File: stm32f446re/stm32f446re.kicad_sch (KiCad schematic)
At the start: 15 parts, among them SW1 SW_Push, SW2 SW_SPDT, U1 STM32F446RETx

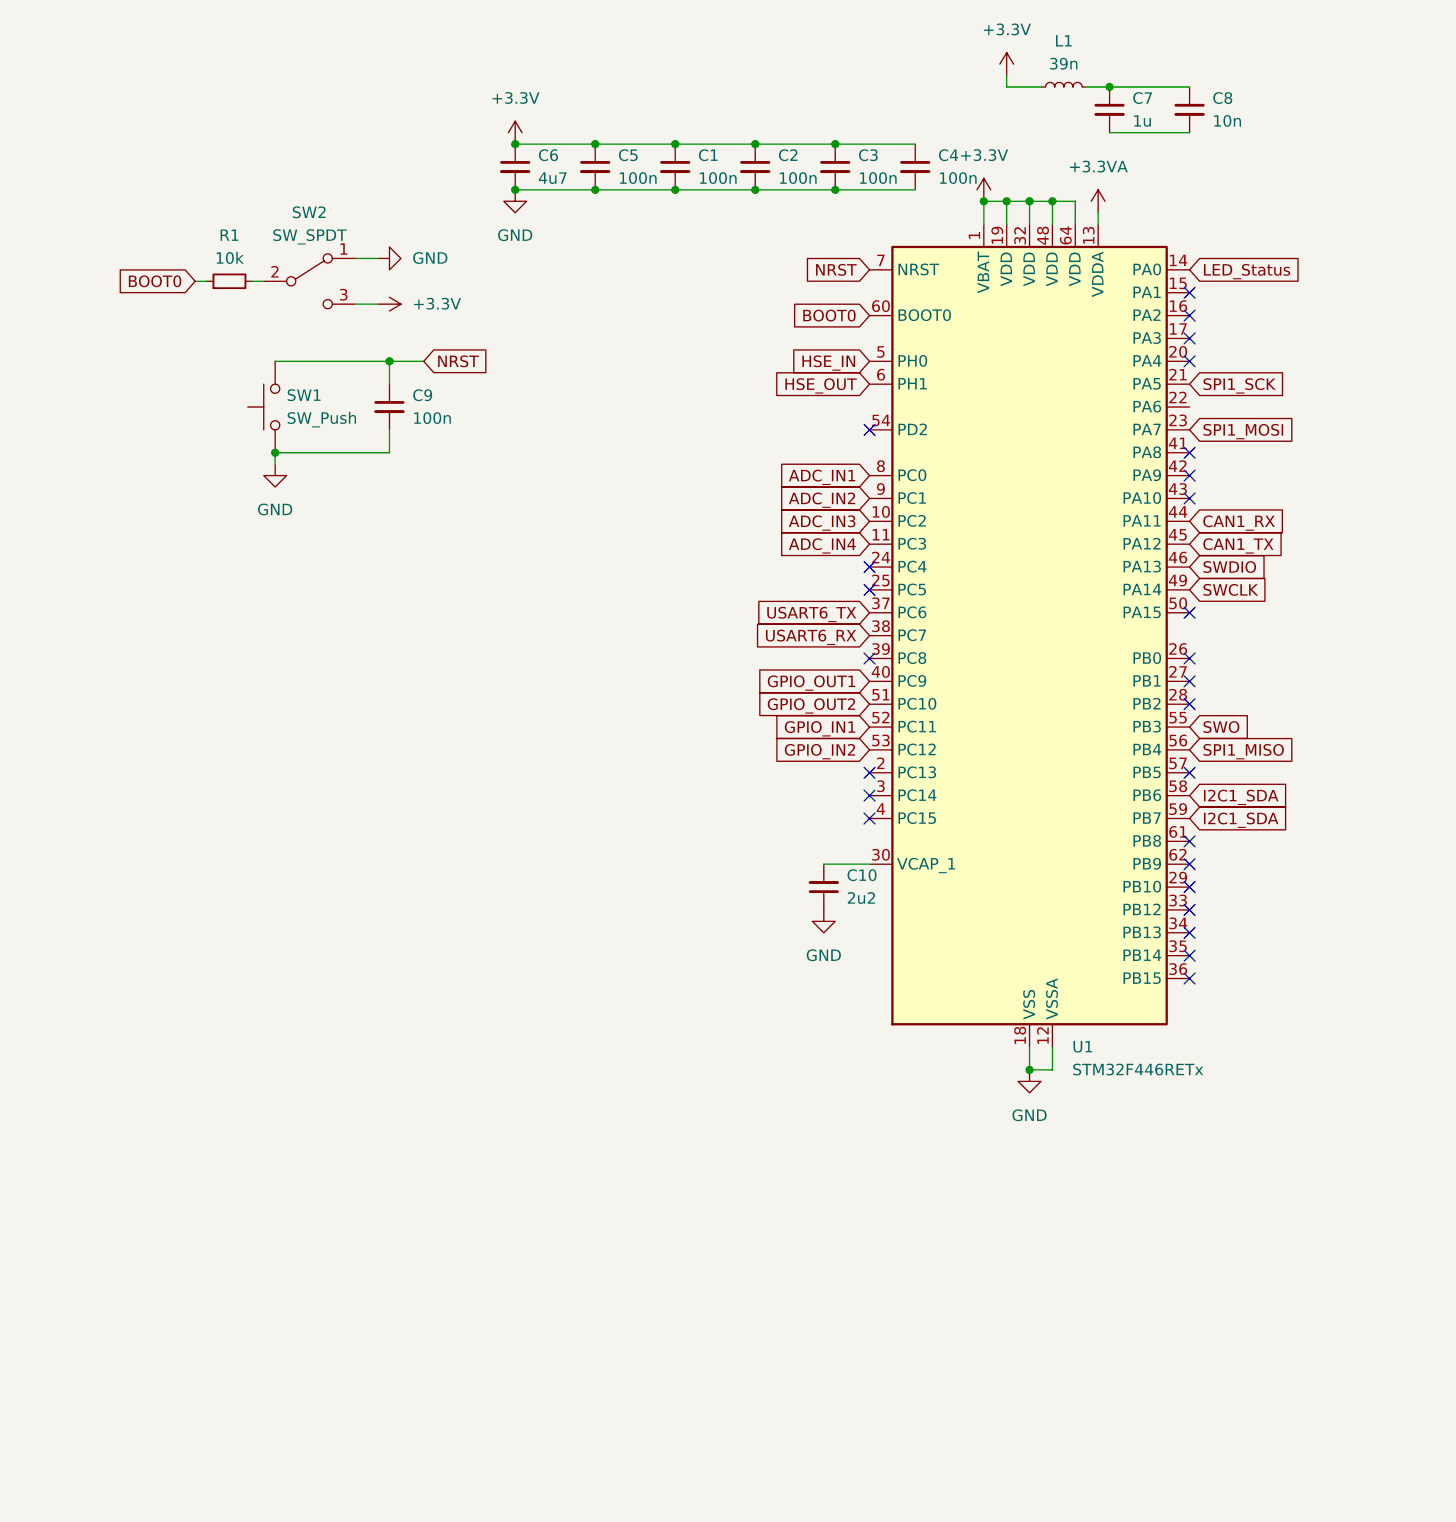
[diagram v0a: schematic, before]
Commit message: Added connectors for the left half of the f446re need to do the right half
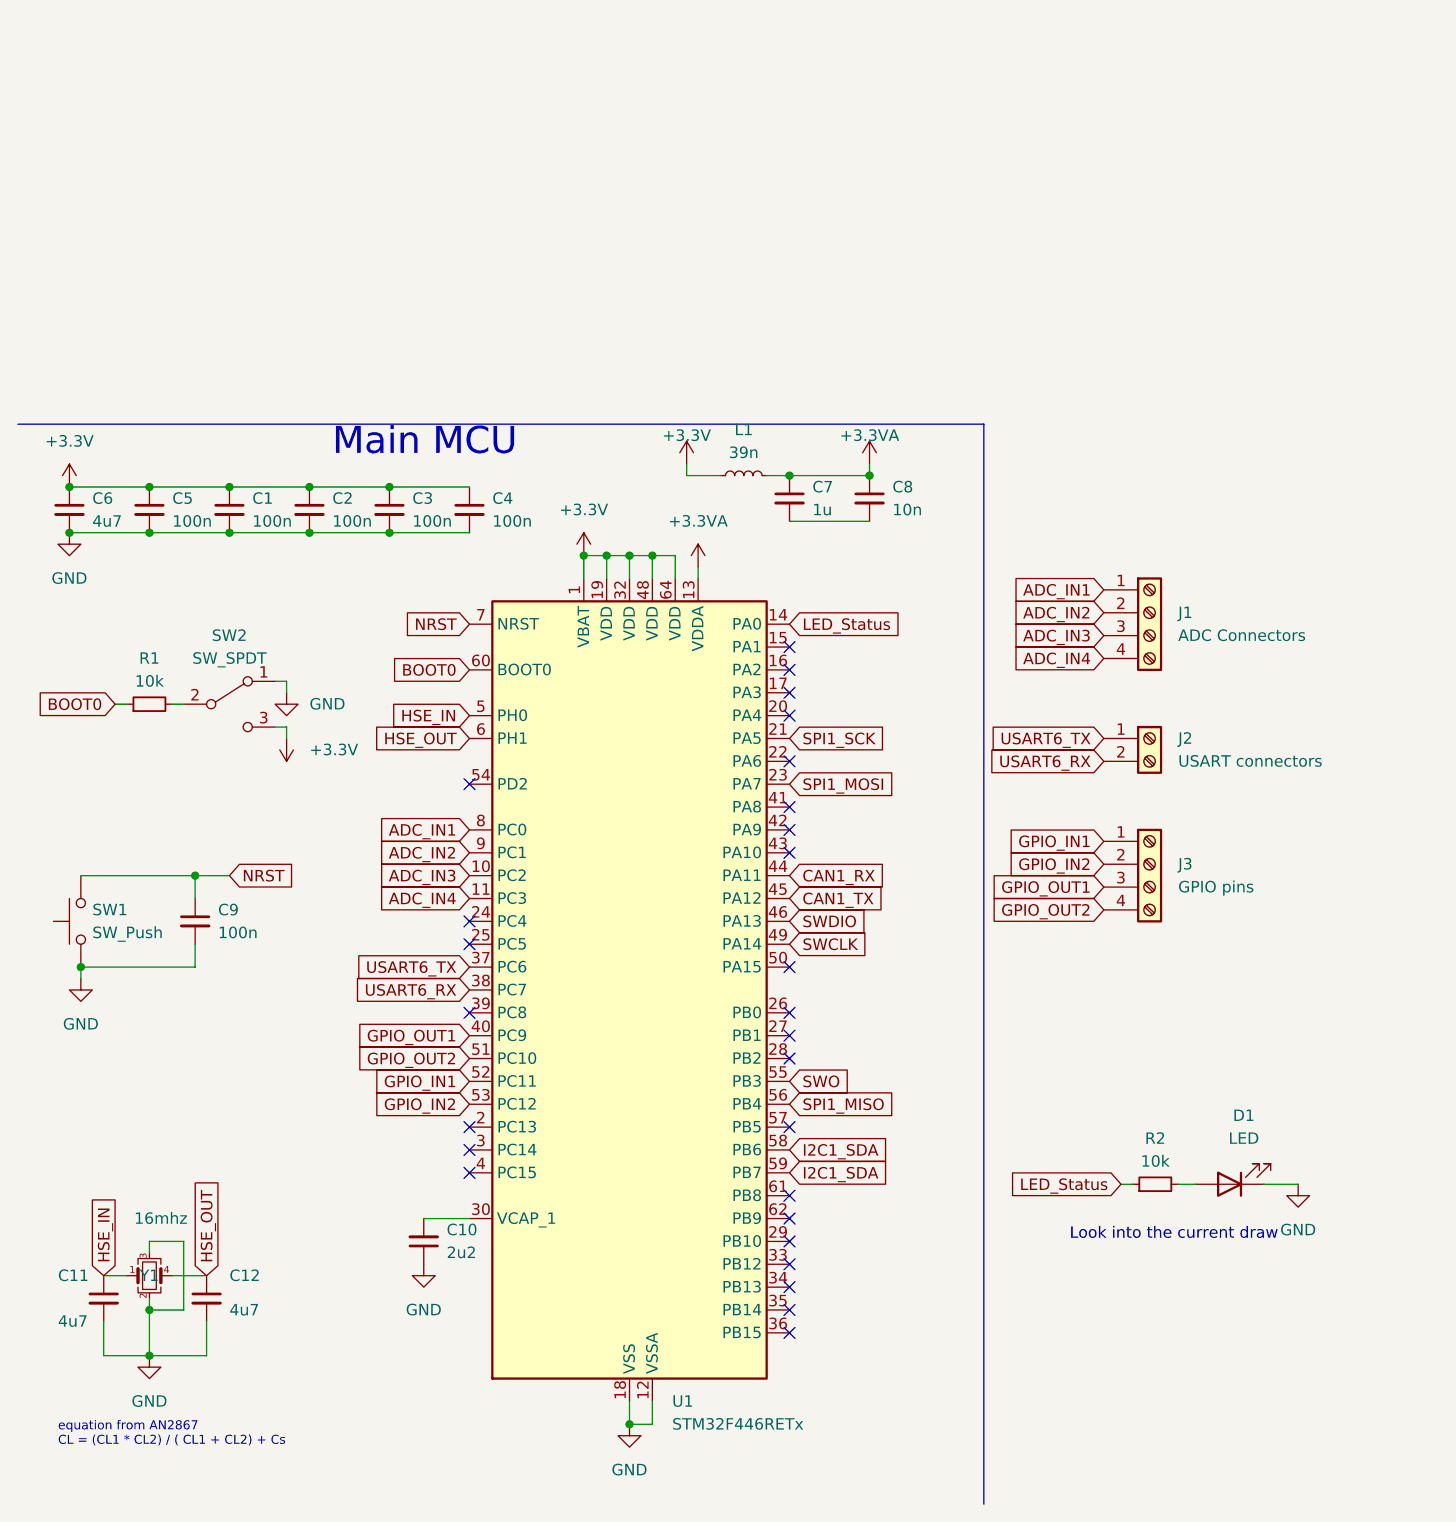
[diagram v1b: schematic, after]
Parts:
- added C11, C12: 4u7, symbol Device:C_Small
- added D1: LED, symbol Device:LED
- added J1: ADC Connectors, TerminalBlock_Phoenix:TerminalBlock_Phoenix_MKDS-1,5-4-5.08_1x04_P5.08mm_Horizontal, symbol Connector:Screw_Terminal_01x04
- added J2: USART connectors, symbol Connector:Screw_Terminal_01x02
- added J3: GPIO pins, symbol Connector:Screw_Terminal_01x04
- added R2: 10k, symbol Device:R_Small
- added Y1: 16mhz, symbol Device:Crystal_GND23_Small
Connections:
- net +3.3VA: now also C7.1, C8.1, L1.2
- net ADC_IN1: now also J1.1 (Pin_1)
- net ADC_IN2: now also J1.2 (Pin_2)
- net ADC_IN3: now also J1.3 (Pin_3)
- net ADC_IN4: now also J1.4 (Pin_4)
- net GND: now also C11.2, C12.2, D1.1 (K), Y1.2, Y1.3
- net GPIO_IN1: now also J3.1 (Pin_1)
- net GPIO_IN2: now also J3.2 (Pin_2)
- net GPIO_OUT1: now also J3.3 (Pin_3)
- net GPIO_OUT2: now also J3.4 (Pin_4)
- net HSE_IN: now also C11.1, Y1.1
- net HSE_OUT: now also C12.1, Y1.4
- net LED_Status: now also R2.1
- net USART6_RX: now also J2.2 (Pin_2)
- net USART6_TX: now also J2.1 (Pin_1)
- new net: D1.2 (A), R2.2
- no-connect marks 26 -> 27
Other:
- note added: "Look into the current draw"
- note added: "Main MCU"
- note added: "equation from AN2867 CL = (CL1 * CL2) / ( CL1 + CL2) + Cs"
- moved on the sheet: C1, C10, C2, C3, C4, C5, C6, C7, C8, C9, L1, R1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

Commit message: finished the schematic for the f446re. However, I forgot to add the name for the serial wire debug on the schematic
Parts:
- added J4: SPI connectors, symbol Connector:Screw_Terminal_01x06
- added J5: CAN connectors, symbol Connector:Screw_Terminal_01x04
- added J7: Screw_Terminal_01x05, symbol Connector:Screw_Terminal_01x05
- J3: value GPIO pins -> GPIO connectors
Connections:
- net +3.3V: now also J4.1 (Pin_1), J5.4 (Pin_4), J7.5 (Pin_5)
- net CAN1_RX: now also J5.2 (Pin_2)
- net CAN1_TX: now also J5.1 (Pin_1)
- net GND: now also J4.2 (Pin_2), J5.3 (Pin_3), J7.4 (Pin_4)
- net SPI1_MISO: now also J4.5 (Pin_5)
- net SPI1_MOSI: now also J4.4 (Pin_4)
- net SPI1_SCK: now also J4.3 (Pin_3)
- net SWCLK: now also J7.3 (Pin_3)
- net SWDIO: now also J7.2 (Pin_2)
- net SWO: now also J7.1 (Pin_1)
- net SPI1_CS: now reaches U1.15 (PA1)
- net SPI1_CS: now also J4.6 (Pin_6)
- net ADC_IN1 renamed Analog1
- net ADC_IN2 renamed Analog2
- net ADC_IN3 renamed Analog3
- net ADC_IN4 renamed Analog4
- no-connect marks 27 -> 26
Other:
- note added: "ADC Pins"
- note added: "CAN Pins"
- note added: "DIGITIAL I/O"
- note added: "SPI Pins"
- note added: "STATUS"
- note added: "USART Pins"
- title: (none) -> STM32 F446RE practice board
- moved on the sheet: D1, J1, J2, J3, R2

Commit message: tweaked oscillator, fixed serial debug names, added i2c connectors. Also don't forget to add a voltage regulator
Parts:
- added J6: I2C connectors, symbol Connector:Screw_Terminal_01x04
- added R3: 47, symbol Device:R_Small
- added R4, R5: 2k2, symbol Device:R_Small
- C11, C12: value 4u7 -> 9pF
- J7: value Screw_Terminal_01x05 -> Serial Debug connectors
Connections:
- net +3.3V: now also J6.4 (Pin_4), R4.2, R5.2
- net GND: now also J6.3 (Pin_3)
- net HSE_OUT: now also R3.2; no longer C12.1, Y1.4
- net I2C1_SDA: now also J6.2 (Pin_2), R4.1; no longer U1.58 (PB6)
- new net: C12.1, R3.1, Y1.4
- new net I2C1_SCL: J6.1 (Pin_1), R5.1, U1.58 (PB6)
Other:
- note added: "I2C pins"
- note added: "No termination resistor is need for this. (no transceiver)"
- note added: "Serial debug pins"
- note added: "equation from AN2867 CL = (CL1 * CL2) / ( CL1 + CL2) + Cs Cl = 9pF and Cs is assumed as 5pF"
- note added: "pullup resistors should be in the range of 2k - 10k"
- note removed: "equation from AN2867 CL = (CL1 * CL2) / ( CL1 + CL2) + Cs"

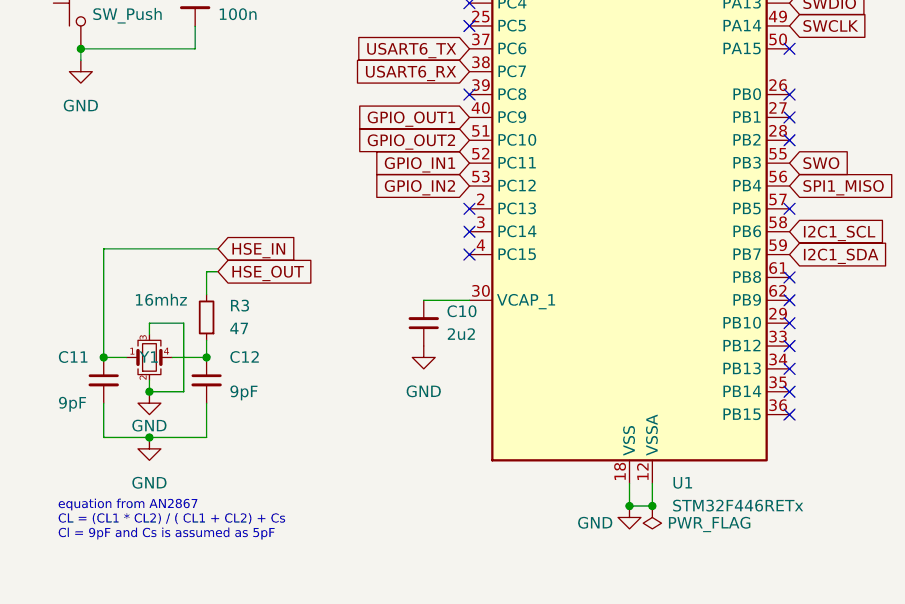
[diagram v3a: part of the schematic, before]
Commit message: adding some mounting holes
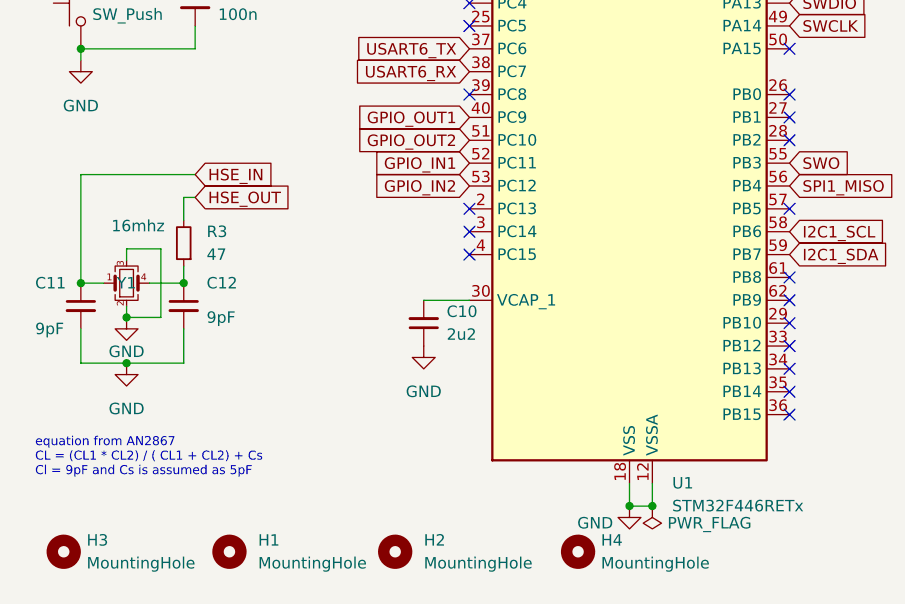
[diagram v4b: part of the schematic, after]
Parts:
- added H1, H2, H3, H4: MountingHole, symbol Mechanical:MountingHole
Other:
- moved on the sheet: C11, C12, R3, Y1
